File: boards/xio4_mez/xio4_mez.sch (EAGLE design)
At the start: 96 parts

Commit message: Start looking at the mezzanine board
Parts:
- removed ARCH_ID: 209-4MS, special:SW_DIP-4
- removed C53, C54, C55, C56, C81: 0.1uF, rcl:C-EUC0201
- removed H3, H6, H7, H8: MOUNT-HOLE4.1, holes:MOUNT-HOLE4.1
- removed LD_0P1, LD_1P, LD_2P, LD_3P, LD_4P: SML-D12D1WT86, led:LEDCHIPLED_0603
- removed MEM_ID: 209-2MS, special:SW_DIP-2
- removed PID: 209-3MS, special:SW_DIP-3
- removed R101, R104, R107, R27, R98: 59R, rcl:R-EU_R0402
- removed R122, R123, R124: 1K, rcl:R-EU_R0201
- removed R14, R15, R16, R17, R18, R6, R7, R8, R9: 47K, rcl:R-EU_R0201
- removed R61, R62, R63, R64, R65: 10K, rcl:R-EU_R0201
- removed SLOT0, SLOT1, SLOT2, SLOT3, SLOT4: PCIE_64, pcie:PCIE_64
- added J1: FPGA, pbxl:BTH-060-01-L-D-A
- added RN1, RN2: 49R9, samacsys:YC124-FR-0749R9L
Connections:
- removed net !LO_CCTL!: SLOT0.A27, SLOT1.A27, SLOT2.A27, SLOT3.A27, SLOT4.A27
- removed net !LO_REF!: SLOT0.B15, SLOT1.B15, SLOT2.B15, SLOT3.B15, SLOT4.B15
- removed net ARCH0: ARCH_ID.1, R9.1
- removed net ARCH1: ARCH_ID.2, R8.1
- removed net ARCH2: ARCH_ID.3, R7.1
- removed net ARCH3: ARCH_ID.4, R6.1
- removed net HBUS0: SLOT0.B18, SLOT1.B18, SLOT2.B18, SLOT3.B18, SLOT4.B18
- removed net HBUS1: SLOT0.B19, SLOT1.B19, SLOT2.B19, SLOT3.B19, SLOT4.B19
- removed net HBUS10: SLOT0.B28, SLOT1.B28, SLOT2.B28, SLOT3.B28, SLOT4.B28
- removed net HBUS11: SLOT0.B29, SLOT1.B29, SLOT2.B29, SLOT3.B29, SLOT4.B29
- removed net HBUS12: SLOT0.B30, SLOT1.B30, SLOT2.B30, SLOT3.B30, SLOT4.B30
- removed net HBUS13: SLOT0.B31, SLOT1.B31, SLOT2.B31, SLOT3.B31, SLOT4.B31
- removed net HBUS2: SLOT0.B20, SLOT1.B20, SLOT2.B20, SLOT3.B20, SLOT4.B20
- removed net HBUS3: SLOT0.B21, SLOT1.B21, SLOT2.B21, SLOT3.B21, SLOT4.B21
- removed net HBUS4: SLOT0.B22, SLOT1.B22, SLOT2.B22, SLOT3.B22, SLOT4.B22
- removed net HBUS5: SLOT0.B23, SLOT1.B23, SLOT2.B23, SLOT3.B23, SLOT4.B23
- removed net HBUS6: SLOT0.B24, SLOT1.B24, SLOT2.B24, SLOT3.B24, SLOT4.B24
- removed net HBUS7: SLOT0.B25, SLOT1.B25, SLOT2.B25, SLOT3.B25, SLOT4.B25
- removed net HBUS8: SLOT0.B26, SLOT1.B26, SLOT2.B26, SLOT3.B26, SLOT4.B26
- removed net HBUS9: SLOT0.B27, SLOT1.B27, SLOT2.B27, SLOT3.B27, SLOT4.B27
- removed net MEM0: MEM_ID.1, R18.1
- removed net MEM1: MEM_ID.2, R17.1
- removed net N$1: LD_0P1.A, R27.2
- removed net N$101: LD_4P.A, R107.2
- removed net N$11: ARCH_ID.5, ARCH_ID.6, ARCH_ID.7, ARCH_ID.8, R122.2
- removed net N$48: MEM_ID.3, MEM_ID.4, R123.2
- removed net N$49: PID.4, PID.5, PID.6, R124.2
- removed net N$91: LD_1P.A, R98.2
- removed net N$94: LD_2P.A, R101.2
- removed net N$97: LD_3P.A, R104.2
- removed net PID0: PID.1, R16.1
- removed net PID1: PID.2, R15.1
- removed net PID2: PID.3, R14.1
- removed net S0_PRESENT: R27.1, R61.2, SLOT0.B4
- removed net S1_PRESENT: R62.2, R98.1, SLOT1.B4
- removed net S2_PRESENT: R101.1, R63.2, SLOT2.B4
- removed net S3_PRESENT: R104.1, R64.2, SLOT3.B4
- removed net S4_PRESENT: R107.1, R65.2, SLOT4.B4
- removed net SPI0_IRQ: SLOT0.A8
- removed net SPI0_MOSI: SLOT0.A9
- removed net SPI1_IRQ: SLOT1.A8
- removed net SPI1_MISO: SLOT1.A10
- removed net SPI1_MOSI: SLOT1.A9
- removed net SPI2_IRQ: SLOT2.A8
- removed net SPI2_MISO: SLOT2.A10
- removed net SPI2_MOSI: SLOT2.A9
- removed net SPI3_IRQ: SLOT3.A8
- removed net SPI3_MISO: SLOT3.A10
- removed net SPI3_MOSI: SLOT3.A9
- removed net SPI4_IRQ: SLOT4.A8
- removed net SPI4_MISO: SLOT4.A10
- removed net SPI4_MOSI: SLOT4.A9
- removed net SPIO_MISO: SLOT0.A10
- removed net VALID_RD: SLOT0.A7, SLOT1.A7, SLOT2.A7, SLOT3.A7, SLOT4.A7
- removed net VALID_WR: SLOT0.A6, SLOT1.A6, SLOT2.A6, SLOT3.A6, SLOT4.A6
- new net TX0_N: CN1G$1.TX0-, J1.IO_B34_LN17(Y19), RN1.3
- new net TX0_P: CN1G$1.TX0+, J1.IO_B34_LP17(Y18), RN1.4
- new net TX1_N: CN1G$1.TX1-, J1.IO_B34_LN18(W16), RN2.1
- new net TX1_P: CN1G$1.TX1+, J1.IO_B34_LP18(V16), RN2.2
- new net TX2_N: CN1G$1.TX2-, J1.IO_B34_LN21(V18), RN2.3
- new net TX2_P: CN1G$1.TX2+, J1.IO_B34_LP21(V17), RN2.4
- new net TXC_N: CN1G$1.TXC-, J1.IO_B34_LN8(Y14), RN1.1
- new net TXC_P: CN1G$1.TXC+, J1.IO_B34_LP8(W14), RN1.2
- new net VCCIO: J1.VDDIO_34_PL@70, J1.VDDIO_34_PL@81, J1.VDDIO_35_PL@19, J1.VDDIO_35_PL@20, RN1.5, RN1.6, RN1.7, RN1.8, RN2.5, RN2.6, RN2.7, RN2.8
- net !LO_EXTSEL!: no longer SLOT0.A29, SLOT1.A29, SLOT2.A29, SLOT3.A29, SLOT4.A29
- net !LO_HALT!: no longer SLOT0.B13, SLOT1.B13, SLOT2.B13, SLOT3.B13, SLOT4.B13
- net !LO_IRQ!: no longer SLOT0.B14, SLOT1.B14, SLOT2.B14, SLOT3.B14, SLOT4.B14
- net !LO_MPD!: no longer SLOT0.A30, SLOT1.A30, SLOT2.A30, SLOT3.A30, SLOT4.A30
- net !LO_RST!: no longer SLOT0.B16, SLOT1.B16, SLOT2.B16, SLOT3.B16, SLOT4.B16
- net +3V3: no longer R122.1, R123.1, R124.1, SLOT1.A3, SLOT2.A2, SLOT3.A2, SLOT3.A3, SLOT4.A1
- net +5V: no longer C53.1, C54.1, C55.1, C56.1, C81.1, SLOT0.B1, SLOT0.B2, SLOT0.B3, SLOT1.B1, SLOT1.B2, SLOT1.B3, SLOT2.B1, SLOT2.B2, SLOT2.B3, SLOT3.B1, SLOT3.B2, SLOT3.B3, SLOT4.B1, SLOT4.B2, SLOT4.B3
- net GND: no longer C53.2, C54.2, C55.2, C56.2, C81.2, LD_0P1.C, LD_1P.C, LD_2P.C, LD_3P.C, LD_4P.C, R14.2, R15.2, R16.2, R17.2, R18.2, R6.2, R61.1, R62.1, R63.1, R64.1, R65.1, R7.2, R8.2, R9.2, SLOT0.A1, SLOT0.A2, SLOT0.A3, SLOT0.A4, SLOT0.A5, SLOT0.B32, SLOT1.A1, SLOT1.A2, SLOT1.A4, SLOT1.A5, SLOT1.B32, SLOT2.A1, SLOT2.A3, SLOT2.A4, SLOT2.A5, SLOT2.B32, SLOT3.A1, SLOT3.A4, SLOT3.A5, SLOT3.B32, SLOT4.A2, SLOT4.A3, SLOT4.A4, SLOT4.A5, SLOT4.B32
- net LO_A0: no longer SLOT0.A11, SLOT1.A11, SLOT2.A11, SLOT3.A11, SLOT4.A11
- net LO_A1: no longer SLOT0.A12, SLOT1.A12, SLOT2.A12, SLOT3.A12, SLOT4.A12
- net LO_A10: no longer SLOT0.A21, SLOT1.A21, SLOT2.A21, SLOT3.A21, SLOT4.A21
- net LO_A11: no longer SLOT0.A22, SLOT1.A22, SLOT2.A22, SLOT3.A22, SLOT4.A22
- net LO_A12: no longer SLOT0.A23, SLOT1.A23, SLOT2.A23, SLOT3.A23, SLOT4.A23
- net LO_A13: no longer SLOT0.A24, SLOT1.A24, SLOT2.A24, SLOT3.A24, SLOT4.A24
- net LO_A14: no longer SLOT0.A25, SLOT1.A25, SLOT2.A25, SLOT3.A25, SLOT4.A25
- net LO_A15: no longer SLOT0.A26, SLOT1.A26, SLOT2.A26, SLOT3.A26, SLOT4.A26
- net LO_A2: no longer SLOT0.A13, SLOT1.A13, SLOT2.A13, SLOT3.A13, SLOT4.A13
- net LO_A3: no longer SLOT0.A14, SLOT1.A14, SLOT2.A14, SLOT3.A14, SLOT4.A14
- net LO_A4: no longer SLOT0.A15, SLOT1.A15, SLOT2.A15, SLOT3.A15, SLOT4.A15
- net LO_A5: no longer SLOT0.A16, SLOT1.A16, SLOT2.A16, SLOT3.A16, SLOT4.A16
- net LO_A6: no longer SLOT0.A17, SLOT1.A17, SLOT2.A17, SLOT3.A17, SLOT4.A17
- net LO_A7: no longer SLOT0.A18, SLOT1.A18, SLOT2.A18, SLOT3.A18, SLOT4.A18
- net LO_A8: no longer SLOT0.A19, SLOT1.A19, SLOT2.A19, SLOT3.A19, SLOT4.A19
- net LO_A9: no longer SLOT0.A20, SLOT1.A20, SLOT2.A20, SLOT3.A20, SLOT4.A20
- net LO_CLK: no longer SLOT0.A28, SLOT1.A28, SLOT2.A28, SLOT3.A28, SLOT4.A28
- net LO_D0: no longer SLOT0.B5, SLOT1.B5, SLOT2.B5, SLOT3.B5, SLOT4.B5
- net LO_D1: no longer SLOT0.B6, SLOT1.B6, SLOT2.B6, SLOT3.B6, SLOT4.B6
- net LO_D2: no longer SLOT0.B7, SLOT1.B7, SLOT2.B7, SLOT3.B7, SLOT4.B7
- net LO_D3: no longer SLOT0.B8, SLOT1.B8, SLOT2.B8, SLOT3.B8, SLOT4.B8
- net LO_D4: no longer SLOT0.B9, SLOT1.B9, SLOT2.B9, SLOT3.B9, SLOT4.B9
- net LO_D5: no longer SLOT0.B10, SLOT1.B10, SLOT2.B10, SLOT3.B10, SLOT4.B10
- net LO_D6: no longer SLOT0.B11, SLOT1.B11, SLOT2.B11, SLOT3.B11, SLOT4.B11
- net LO_D7: no longer SLOT0.B12, SLOT1.B12, SLOT2.B12, SLOT3.B12, SLOT4.B12
- net LO_R/!W!: no longer SLOT0.B17, SLOT1.B17, SLOT2.B17, SLOT3.B17, SLOT4.B17
- net LO_RD4: no longer SLOT0.A31, SLOT1.A31, SLOT2.A31, SLOT3.A31, SLOT4.A31
- net LO_RD5: no longer SLOT0.A32, SLOT1.A32, SLOT2.A32, SLOT3.A32, SLOT4.A32
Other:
- note added: "2 1 0 N"
- note removed: "+5V Card-present Slot ID GND"
- note removed: "+5V Slot 3.3v Card-present Slot ID GND"
- note removed: "2-way and 4-way DIPs not at Seeed"
- note removed: "Amber and Red LEDs are configured for 10mA current"
- note removed: "Architecture selection"
- note removed: "B1,2,3 B4 A1,2,3 A4,5,6,7"
- note removed: "B1,2,3 B5,6,7 B4 A1,2,3 A4,5,6,7"
- note removed: "Board Config"
- note removed: "Green and Orange LEDs are configured for 20mA current"
- note removed: "LED resistor values"
- note removed: "Memory-emulation selection"
- note removed: "Orange LED"
- note removed: "Peripheral-ID selection"
- note removed: "SD Card"
- note removed: "Serial & Config"
- note removed: "Slot 4"
- note removed: "Slot id: 0,0,0"
- note removed: "Slot id: 0,0,1"
- note removed: "Slot id: 0,1,0"
- note removed: "Slot id: 0,1,1"
- note removed: "Slots 0,1"
- note removed: "Slots 2,3"

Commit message: Add the HDMI stage
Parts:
- removed RN1, RN2: 49R9, samacsys:YC124-FR-0749R9L
- added C10, C19, C20, C21, C22, C7: 0.1uF, rcl:C-EUC0201
- added D1: RB751V40,115, microbuilder:DIODESOD-323
- added D2: RED-0805, Seeed-LED:SMD-LED-CLEAR-RED(0805)
- added IC1: SN74LVC2G07DCKR, samacsys:SN74LVC2G07DCKR
- added IC2: SN74LVC1G07MDCKREP, samacsys:SN74LVC1G07MDCKREP
- added IC3: NL17SZ126XV5T2G, samacsys:NL17SZ126XV5T2G
- added IC4: TPS2051BDBVR, samacsys:TPS2051BDBVR
- added Q1: SMMBT3904LT1G, samacsys:SMMBT3904LT1G
- added R1, R11, R12, R14, R6, R7, R8, R9: 49R9, rcl:R-EU_R0201
- added R15: 27K, rcl:R-EU_R0201
- added R16, R17: 1K5, rcl:R-EU_R0201
- added R18, R20: 4K7, rcl:R-EU_R0201
- added R23, R27: 100K, rcl:R-EU_R0201
- added R24, R28, R30: 1K, rcl:R-EU_R0201
- added R29, R31, R32: 10K, rcl:R-EU_R0201
- added R33: 820R, rcl:R-EU_R0201
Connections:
- new net HDMI_CEC: CN1G$1.CEC, D1.C, J1.IO_B34_LN20(R18)
- new net HDMI_DET_IO: IC3.INA, J1.IO_B34_LP16(V20), R24.2, R27.2
- new net HDMI_OUT_EN: J1.IO_B34_LN15(U20), R30.1, R32.2
- new net HDMI_SCL: IC1.1A, J1.IO_B34_LP20(T17), R18.2
- new net HDMI_SDA: IC1.2A, J1.IO_B34_LN16(W20), R20.2
- new net HPD: CN1G$1.HOTPLUG, IC2.A, R23.2, R28.2
- new net N$1: CN1G$1.DDAT, IC1.1Y, R17.1
- new net N$10: D2.-, R33.2
- new net N$2: D1.A, R15.1
- new net N$3: CN1G$1.DCLK, IC1.2Y, R16.1
- new net N$4: IC3.OE, Q1.C, R29.2
- new net N$5: IC2.Y, R24.1
- new net N$6: IC3.OUTY, R28.1
- new net N$7: Q1.B, R30.2, R31.1
- new net N$8: C21.1, IC4.!EN, R32.1
- new net N$9: IC4.!OC, R33.1
- new net V+: C22.1, C7.1, CN1G$1.+5V, IC4.OUT, R16.2, R17.2
- net +5V: now also C20.1, IC4.IN
- net GND: now also C10.2, C19.2, C20.2, C21.2, C22.2, C7.2, CN1G$1.GND, CN1G$1.TX0_SHIELD, CN1G$1.TX1_SHIELD, CN1G$1.TX2_SHIELD, CN1G$1.TXC_SHIELD, IC1.GND, IC2.GND, IC3.GND, IC4.GND, Q1.E, R23.1, R27.1, R31.2
- net TX0_N: now also R1.2; no longer RN1.3
- net TX0_P: now also R6.2; no longer RN1.4
- net TX1_N: now also R7.2; no longer RN2.1
- net TX1_P: now also R8.2; no longer RN2.2
- net TX2_N: now also R9.2; no longer RN2.3
- net TX2_P: now also R11.2; no longer RN2.4
- net TXC_N: now also R12.2; no longer RN1.1
- net TXC_P: now also R14.2; no longer RN1.2
- net VCCIO: now also C10.1, C19.1, D2.+, IC1.VCC, IC2.VCC, IC3.VCC, R1.1, R11.1, R12.1, R14.1, R15.2, R18.1, R20.1, R29.1, R6.1, R7.1, R8.1, R9.1; no longer RN1.5, RN1.6, RN1.7, RN1.8, RN2.5, RN2.6, RN2.7, RN2.8
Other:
- note removed: "2 1 0 N"

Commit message: Use the corrected footprint for the Mezzanine board, and route the HDMI critical signals.
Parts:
- removed J1: FPGA, pbxl:BTH-060-01-L-D-A
- added U$1: BTH-060-01-F-D-A, pbxl:BTH-060-01-F-D-A
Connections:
- net HDMI_CEC: no longer J1.IO_B34_LN20(R18)
- net HDMI_DET_IO: now also U$1.IO_B34_LP7(Y16); no longer J1.IO_B34_LP16(V20)
- net HDMI_OUT_EN: now also U$1.IO_B34_LN7(Y17); no longer J1.IO_B34_LN15(U20)
- net HDMI_SCL: now also U$1.IO_B34_LN10(W15); no longer J1.IO_B34_LP20(T17)
- net HDMI_SDA: now also U$1.IO_B34_LP10(V15); no longer J1.IO_B34_LN16(W20)
- net TX0_N: now also U$1.IO_B34_LN22(W19); no longer J1.IO_B34_LN17(Y19)
- net TX0_P: now also U$1.IO_B34_LP22(W18); no longer J1.IO_B34_LP17(Y18)
- net TX1_N: now also U$1.IO_B34_LN12(U19); no longer J1.IO_B34_LN18(W16)
- net TX1_P: now also U$1.IO_B34_LP12(U18); no longer J1.IO_B34_LP18(V16)
- net TX2_N: now also U$1.IO_B34_LN9(U17); no longer J1.IO_B34_LN21(V18)
- net TX2_P: now also U$1.IO_B34_LP9(T16); no longer J1.IO_B34_LP21(V17)
- net TXC_N: now also U$1.IO_B34_LN11(U15); no longer J1.IO_B34_LN8(Y14)
- net TXC_P: now also U$1.IO_B34_LP11(U14); no longer J1.IO_B34_LP8(W14)
- net VCCIO: now also U$1.VDDIO_34_PL@70, U$1.VDDIO_34_PL@81, U$1.VDDIO_35_PL@19, U$1.VDDIO_35_PL@20; no longer J1.VDDIO_34_PL@70, J1.VDDIO_34_PL@81, J1.VDDIO_35_PL@19, J1.VDDIO_35_PL@20

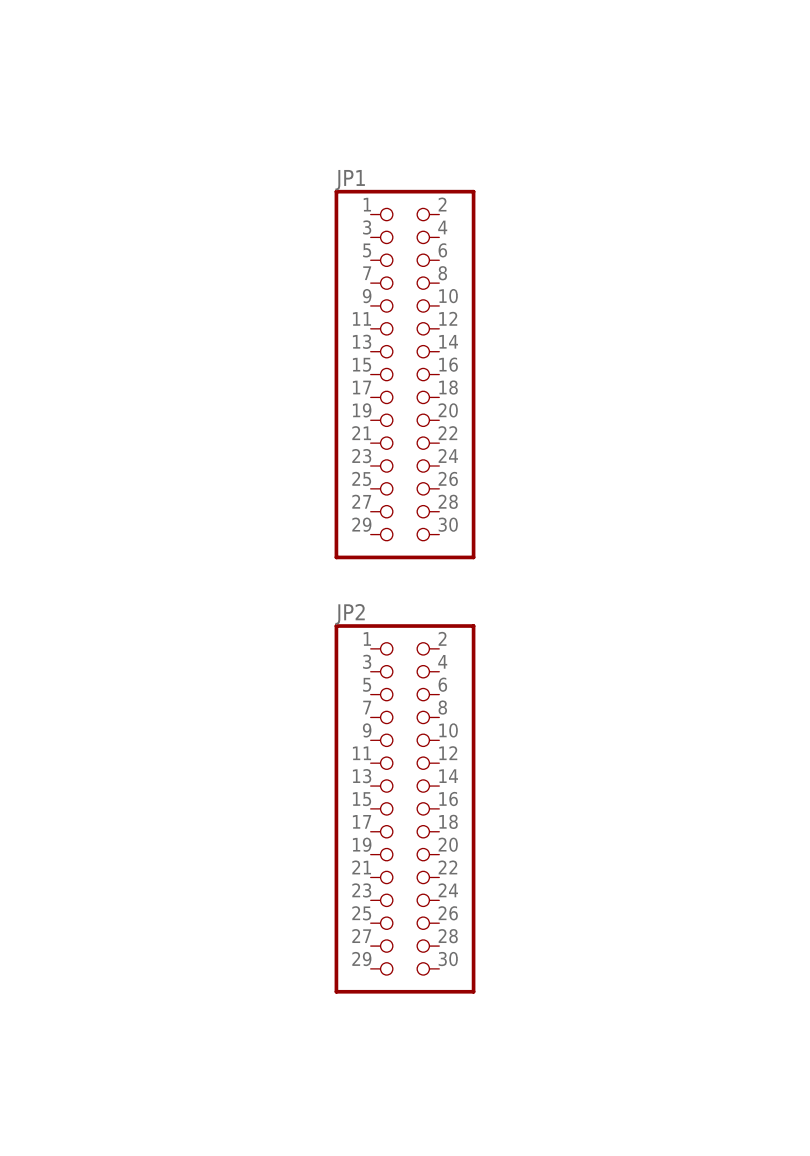
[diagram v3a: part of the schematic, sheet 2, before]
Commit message: Add the SPI routing
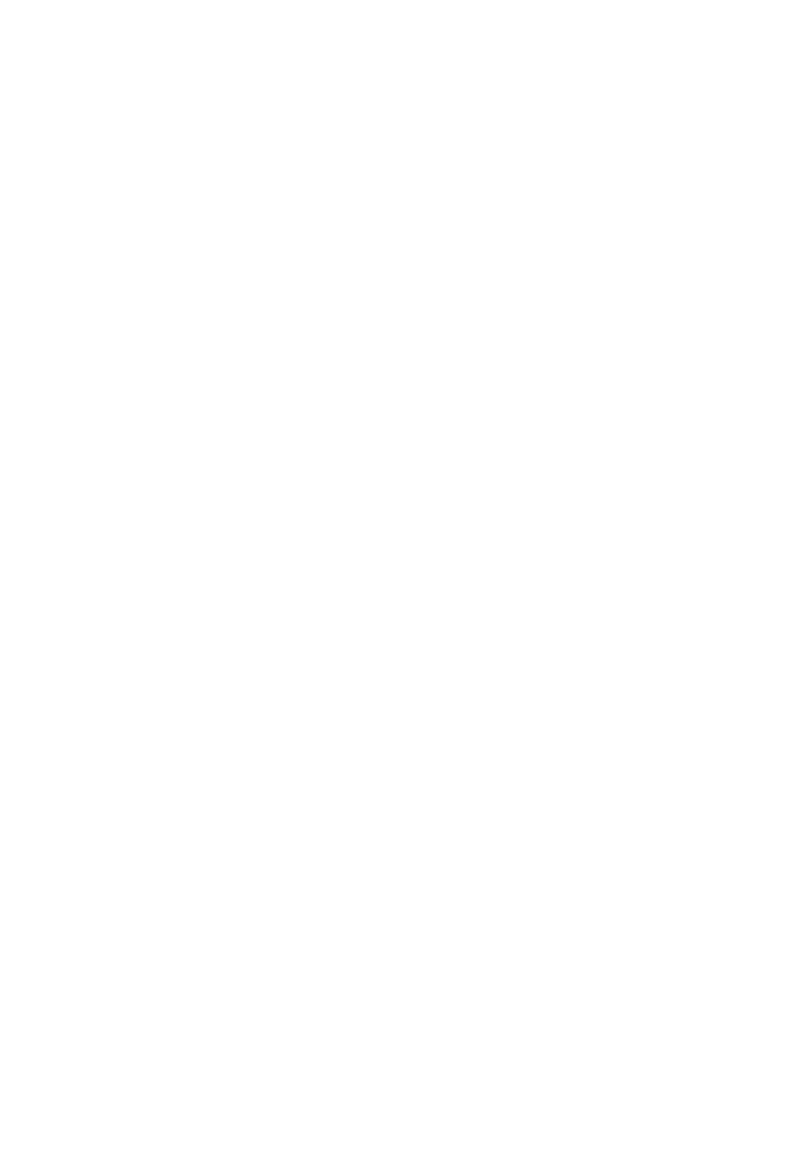
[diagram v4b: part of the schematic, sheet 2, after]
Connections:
- new net SPI0_CLK: JP1.7, U$1.IO_B34_LN14(P20)
- new net SPI0_MISO: JP1.8, U$1.IO_B34_LP14(N20)
- new net SPI0_MOSI: JP1.9, U$1.IO_B34_LN13(P19)
- new net SPI1_CLK: JP1.10, U$1.IO_B34_LP13(N18)
- new net SPI1_MISO: JP1.11, U$1.IO_B35_LN7(M20)
- new net SPI1_MOSI: JP1.12, U$1.IO_B35_LP7(M19)
- new net SPI_SS0: JP1.13, U$1.IO_B34_LN23(P18)
- new net SPI_SS1: JP1.14, U$1.IO_B34_LP23(N17)
- new net SPI_SS2: JP1.15, U$1.IO_B35_LN8(M18)
- new net SPI_SS3: JP1.16, U$1.IO_B35_LP8(M17)
- new net SPI_SS4: JP1.17, U$1.IO_B35_LN24(J16)
- new net SPI_SS5: JP1.18, U$1.IO_B35_LP24(K16)
- net !LO_EXTSEL!: now also JP2.6
- net !LO_HALT!: now also JP2.8
- net !LO_IRQ!: now also JP2.10
- net !LO_MPD!: now also JP2.12
- net !LO_RST!: now also JP1.5
- net GND: now also U$1.GND@101, U$1.GND@102, U$1.GND@111, U$1.GND@112, U$1.GND@113, U$1.GND@17, U$1.GND@18, U$1.GND@20, U$1.GND@29, U$1.GND@39, U$1.GND@40, U$1.GND@49, U$1.GND@50, U$1.GND@59, U$1.GND@60, U$1.GND@69, U$1.GND@7, U$1.GND@72, U$1.GND@79, U$1.GND@8, U$1.GND@82, U$1.GND@91, U$1.GND@92
- net LO_A0: now also JP2.1
- net LO_A1: now also JP2.3
- net LO_A10: now also JP2.21
- net LO_A11: now also JP2.23
- net LO_A12: now also JP2.25
- net LO_A13: now also JP2.27
- net LO_A14: now also JP2.29
- net LO_A15: now also JP2.30
- net LO_A2: now also JP2.5
- net LO_A3: now also JP2.7
- net LO_A4: now also JP2.9
- net LO_A5: now also JP2.11
- net LO_A6: now also JP2.13
- net LO_A7: now also JP2.15
- net LO_A8: now also JP2.17
- net LO_A9: now also JP2.19
- net LO_CLK: now also JP2.2
- net LO_D0: now also JP2.14
- net LO_D1: now also JP2.16
- net LO_D2: now also JP2.18
- net LO_D3: now also JP2.20
- net LO_D4: now also JP2.22
- net LO_D5: now also JP2.24
- net LO_D6: now also JP2.26
- net LO_D7: now also JP2.28
- net LO_R/!W!: now also JP2.4
- net LO_RD4: now also JP1.1
- net LO_RD5: now also JP1.3

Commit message: First pass at a “finished” board
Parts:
- added JP3: (no value), pinhead-2:PINHD-2X15_2.54-SMD
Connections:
- new net HBUS0: JP3.2, U$1.IO_B35_LP17(J20)
- new net HBUS1: JP3.1, U$1.IO_B35_LN17(H20)
- new net HBUS10: JP3.12, U$1.IO_B35_LP13(H16)
- new net HBUS11: JP3.11, U$1.IO_B35_LN13(H17)
- new net HBUS12: JP3.14, U$1.IO_B35_LP22(L14)
- new net HBUS13: JP3.13, U$1.IO_B35_LN22(L15)
- new net HBUS14: JP3.16, U$1.IO_B35_LP23(M14)
- new net HBUS15: JP3.15, U$1.IO_B35_LN23(M15)
- new net HBUS16: JP3.18, U$1.IO_B34_LP24(P15)
- new net HBUS17: JP3.17, U$1.IO_B34_LN24(P16)
- new net HBUS18: JP3.20, U$1.IO_B35_LP21(N15)
- new net HBUS19: JP3.19, U$1.IO_B35_LN21(N16)
- new net HBUS2: JP3.4, U$1.IO_B35_LP12(K17)
- new net HBUS20: JP3.22, U$1.IO_B34_LP19(R16)
- new net HBUS21: JP3.21, U$1.IO_B34_LN19(R17)
- new net HBUS22: JP3.24, U$1.IO_B34_LP15(T20)
- new net HBUS23: JP3.23, U$1.IO_B34_LN15(U20)
- new net HBUS24: JP3.26, U$1.IO_B34_LP16(V20)
- new net HBUS25: JP3.25, U$1.IO_B34_LN16(W20)
- new net HBUS26: JP3.28, U$1.IO_B34_LP20(T17)
- new net HBUS27: JP3.27, U$1.IO_B34_LN20(R18)
- new net HBUS3: JP3.3, U$1.IO_B35_LN12(K18)
- new net HBUS4: JP3.6, U$1.IO_B35_LP10(K19)
- new net HBUS5: JP3.5, U$1.IO_B35_LN10(J19)
- new net HBUS6: JP3.8, U$1.IO_B35_LP19(H15)
- new net HBUS7: JP3.7, U$1.IO_B35_LN19(G15)
- new net HBUS8: JP3.10, U$1.IO_B35_LP20(K14)
- new net HBUS9: JP3.9, U$1.IO_B35_LN20(J14)
- new net PRESENT0: JP1.25, U$1.IO_B35_LN6(F17)
- new net PRESENT1: JP1.26, U$1.IO_B35_LP6(F16)
- new net PRESENT2: JP1.27, U$1.IO_B35_LN4(D20)
- new net PRESENT3: JP1.28, U$1.IO_B35_LP4(D19)
- new net PRESENT4: JP1.29, U$1.IO_B35_LN3(D18)
- new net PRESENT5: JP1.30, U$1.IO_B35_LP3(E17)
- new net SPI_IRQ0: JP1.19, U$1.IO_B35_LN9(L20)
- new net SPI_IRQ1: JP1.20, U$1.IO_B35_LP9(L19)
- new net SPI_IRQ2: JP1.21, U$1.IO_B35_LN11(L17)
- new net SPI_IRQ3: JP1.22, U$1.IO_B35_LP11(L16)
- new net SPI_IRQ4: JP1.23, U$1.IO_B35_LN15(F20)
- new net SPI_IRQ5: JP1.24, U$1.IO_B35_LP15(F19)
- new net VALID_RD: JP1.4, U$1.IO_B34_LN8(Y14)
- new net VALID_WR: JP1.6, U$1.IO_B34_LP8(W14)
- net +5V: now also JP1.2, JP3.29, JP3.30
- net DIR_A: now also U$1.IO_B35_LN18(G20)
- net DIR_CLK: now also U$1.IO_B35_LN1(B20)
- net DIR_D: now also U$1.IO_B35_LP18(G19)
- net DIR_EXTSEL: now also U$1.IO_B35_LP1(C20)
- net DIR_HALT: now also U$1.IO_B35_LN14(H18)
- net DIR_IRQ: now also U$1.IO_B35_LP14(J18)
- net DIR_MPD: now also U$1.IO_B35_LN16(G18)
- net DIR_RD4: now also U$1.IO_B35_LP16(G17)
- net DIR_RD5: now also U$1.IO_B35_LN5(E19)
- net DIR_RST: now also U$1.IO_B35_LP5(E18)
- net DIR_RW: now also U$1.IO_B35_LN2(A20)
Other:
- moved on the sheet: JP1, JP2
